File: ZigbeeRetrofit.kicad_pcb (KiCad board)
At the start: 2 copper layers, 20 x 50 mm, 24 parts, among them J1 110990030, J2 U.FL-R-SMT-1(10), J3 TC2050-IDC-NL, U1 CC2531F256RHAT, U2 SPX3819M5-L-3-3, Y1 32 Mhz, Y2 ECS-.327-12.5-34RR-TR

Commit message: Updated layout with 3d models
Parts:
- moved J3 19.3 mm to (107.4, 58.8), turned to 90 degrees
- moved C7 7.81 mm to (117.3, 77.4)
- moved C2 7.39 mm to (116.4, 68.3), turned to 0 degrees
- moved C6 7.15 mm to (113.0, 73.2)
- moved L1 7.15 mm to (116.5, 72.2)
- moved L2 7.15 mm to (113.0, 71.2)
- moved U1 7.15 mm to (104.5, 74.7)
- moved Y1 7.15 mm to (117.7, 80.5)
- moved C8 7.15 mm to (102.2, 69.1)
- moved R1 7.15 mm to (109.8, 72.3)
- moved C4 6.85 mm to (118.0, 84.0)
- moved C3 6.84 mm to (116.5, 74.6)
- moved C5 6.84 mm to (113.0, 74.6)
- moved C12 6.79 mm to (105.0, 63.6)
- moved Y2 6.79 mm to (106.3, 66.8)
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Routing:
- net /RESET: track 0.00 -> 51.9 mm, vias 0 -> 2
- net /DC: track 0.00 -> 20.5 mm, vias 0 -> 2
- net /DD: track 0.00 -> 19.1 mm
- net Net-(C1-Pad1): track 18.1 -> 29.5 mm
- net /TX: track 29.7 -> 22.5 mm
- net /RX: track 27.8 -> 20.7 mm
- net +5V: track 32.1 -> 36.0 mm
- net Net-(C2-Pad1): track 3.95 -> 6.68 mm
- net +3.3V: track 48.0 -> 49.4 mm, vias 5 -> 6
- net Net-(C7-Pad1): track 12.9 -> 12.3 mm
- net Net-(C11-Pad1): track 7.45 -> 8.12 mm
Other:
- outline, holes or cut-outs redrawn

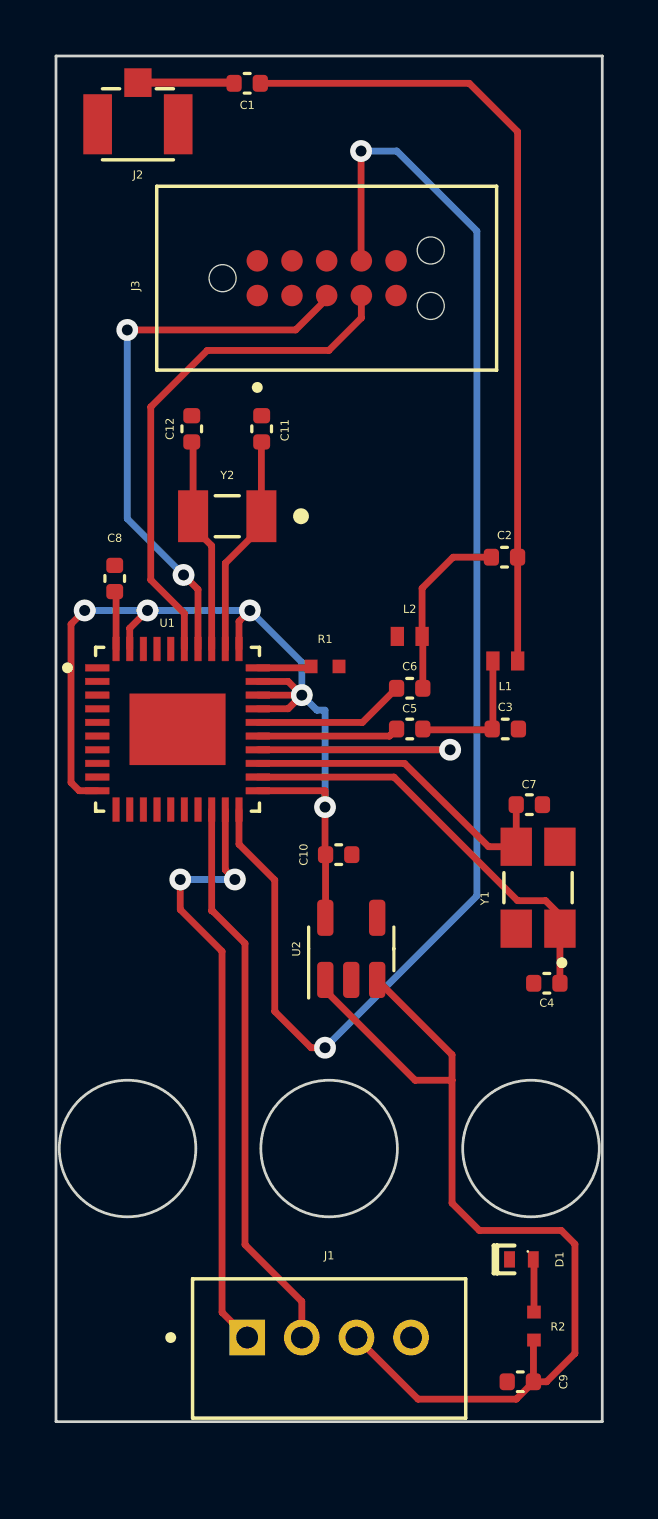
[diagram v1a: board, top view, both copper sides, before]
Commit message: Added ground
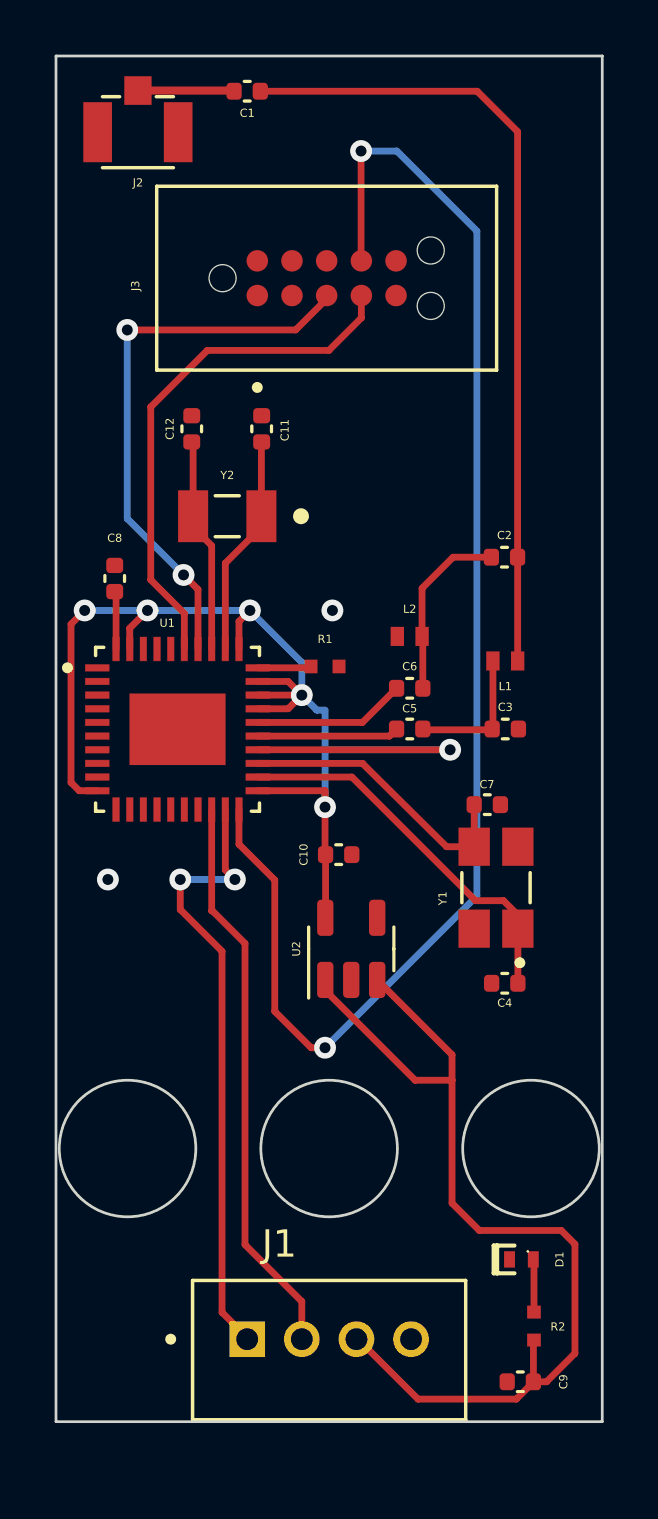
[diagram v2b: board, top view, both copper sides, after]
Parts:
- moved Y1 1.54 mm to (116.1, 80.5)
- moved C4 1.54 mm to (116.4, 84.0)
- moved C7 1.54 mm to (115.8, 77.4)
- moved C1 0.29 mm to (107.0, 51.3)
- moved J2 0.29 mm to (103.0, 52.8)
- moved J1 0.06 mm to (110.0, 97.0)
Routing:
- net Net-(C4-Pad1): track 15.7 -> 14.1 mm
- net Net-(C7-Pad1): track 12.3 -> 10.7 mm
- net GND: vias 0 -> 2
- added copper zone on B.Cu, net GND
- added copper zone on F.Cu, net GND
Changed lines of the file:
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@@
   )
   (footprint "Capacitor_SMD:C_0402_1005Metric" (layer "F.Cu")
-    (at 117.33 77.41)
+    (at 115.79 77.41)
     (descr "Capacitor SMD 0402 (1005 Metric), square (rectangular) end terminal, IPC_7351 nominal, (Body size source: IPC-SM-782 page 76, https://www.pcb-3d.com/wordpress/wp-content/uploads/ipc-sm-782a_amendment_1_and_2.pdf), generated with kicad-footprint-generator")
     (tags "capacitor")
@@
   )
   (footprint "ECS-320-13-42-CKM-TR:XTAL_ECS-320-13-42-CKM-TR" (layer "F.Cu")
-    (at 117.65 80.45 90)
+    (at 116.11 80.45 90)
     (property "MANUFACTURER" "ECS Inc.")
     (property "PARTREV" "11/11")
@@
   )
   (footprint "110990030:SEEED_110990030" (layer "F.Cu")
-    (at 110 96.92)
+    (at 110 96.98)
+    (property "Availability" "In Stock")
+    (property "Check_prices" "https://www.snapeda.com/parts/114020164/Seeed+Technology+Co.%252C+Ltd/view-part/?ref=eda")
+    (property "Description" "\nGROVE FEMALE HEADER R/A 20PACK\n")
     (property "MANUFACTURER" "Seeed Technology")
     (property "MAXIMUM_PACKAGE_HEIGHT" "8.1mm")
+    (property "MF" "Seeed Technology Co., Ltd")
+    (property "MP" "114020164")
     (property "PARTREV" "A")
+    (property "Package" "None")
+    (property "Price" "None")
+    (property "Purchase-URL" "https://www.snapeda.com/api/url_track_click_mouser/?unipart_id=5310052&manufacturer=Seeed Technology Co., Ltd&part_name=114020164&search_term=None")
     (property "STANDARD" "Manufacturer Recommendations")
     (property "Sheetfile" "ZigbeeRetrofit.kicad_sch")
     (property "Sheetname" "")
+    (property "SnapEDA_Link" "https://www.snapeda.com/parts/114020164/Seeed+Technology+Co.%252C+Ltd/view-part/?ref=snap")
     (attr through_hole)
-    (fp_text reference "J1" (at 0 -3) (layer "F.SilkS")
-      (effects (font (size 0.3 0.3) (thickness 0.05)))
+    (fp_text reference "J1" (at -1.825 -3.485) (layer "F.SilkS")
+      (effects (font (size 1 1) (thickness 0.15)))
     )
     (fp_text value "110990030" (at 4.525 4.385) (layer "F.Fab")
       (effects (font (size 1 1) (thickness 0.15)))
     )
+    (fp_line (start -5 2.95) (end -5 -2.15) (layer "F.SilkS") (width 0.127))
+    (fp_line (start 5 2.95) (end -5 2.95) (layer "F.SilkS") (width 0.127))
     (fp_line (start -5 -2.15) (end 5 -2.15) (layer "F.SilkS") (width 0.127))
-    (fp_line (start -5 2.95) (end -5 -2.15) (layer "F.SilkS") (width 0.127))
     (fp_line (start 5 -2.15) (end 5 2.95) (layer "F.SilkS") (width 0.127))
-    (fp_line (start 5 2.95) (end -5 2.95) (layer "F.SilkS") (width 0.127))
     (fp_circle (center -5.8 0) (end -5.7 0) (layer "F.SilkS") (width 0.2) (fill none))
     (fp_line (start -5.25 -2.4) (end 5.25 -2.4) (layer "F.CrtYd") (width 0.05))
@@
     (fp_line (start 5.25 -2.4) (end 5.25 3.2) (layer "F.CrtYd") (width 0.05))
     (fp_line (start 5.25 3.2) (end -5.25 3.2) (layer "F.CrtYd") (width 0.05))
+    (fp_line (start -5 -2.15) (end 5 -2.15) (layer "F.Fab") (width 0.127))
+    (fp_line (start 5 -2.15) (end 5 2.95) (layer "F.Fab") (width 0.127))
+    (fp_line (start -5 2.95) (end -5 -2.15) (layer "F.Fab") (width 0.127))
     (fp_line (start 5 2.95) (end -5 2.95) (layer "F.Fab") (width 0.127))
-    (fp_line (start 5 -2.15) (end 5 2.95) (layer "F.Fab") (width 0.127))
-    (fp_line (start -5 -2.15) (end 5 -2.15) (layer "F.Fab") (width 0.127))
-    (fp_line (start -5 2.95) (end -5 -2.15) (layer "F.Fab") (width 0.127))
     (fp_circle (center -5.8 0) (end -5.7 0) (layer "F.Fab") (width 0.2) (fill none))
     (pad "1" thru_hole rect locked (at -3 0) (size 1.308 1.308) (drill 0.8) (layers *.Cu *.Mask)
@@
     (pad "4" thru_hole circle locked (at 3 0) (size 1.308 1.308) (drill 0.8) (layers *.Cu *.Mask)
       (net 5 "GND") (pinfunction "4") (pintype "passive"))
-    (model "${KIPRJMOD}/110990030/110990030--3DModel-STEP-56544.STEP"
-      (offset (xyz 0 0 0))
-      (scale (xyz 1 1 1))
-      (rotate (xyz -90 0 0))
-    )
   )
   (footprint "Capacitor_SMD:C_0402_1005Metric" (layer "F.Cu")
@@
   )
   (footprint "Capacitor_SMD:C_0402_1005Metric" (layer "F.Cu")
-    (at 107 51 180)
+    (at 107 51.29 180)
     (descr "Capacitor SMD 0402 (1005 Metric), square (rectangular) end terminal, IPC_7351 nominal, (Body size source: IPC-SM-782 page 76, https://www.pcb-3d.com/wordpress/wp-content/uploads/ipc-sm-782a_amendment_1_and_2.pdf), generated with kicad-footprint-generator")
     (tags "capacitor")
@@
   )
   (footprint "Capacitor_SMD:C_0402_1005Metric" (layer "F.Cu")
-    (at 117.97 83.95 180)
+    (at 116.43 83.95 180)
     (descr "Capacitor SMD 0402 (1005 Metric), square (rectangular) end terminal, IPC_7351 nominal, (Body size source: IPC-SM-782 page 76, https://www.pcb-3d.com/wordpress/wp-content/uploads/ipc-sm-782a_amendment_1_and_2.pdf), generated with kicad-footprint-generator")
     (tags "capacitor")
@@
   )
   (footprint "U:HRS_U.FL-R-SMT-1(10)" (layer "F.Cu")
-    (at 103 52.5 180)
+    (at 103 52.79 180)
     (property "AVAILABILITY" "Good")
     (property "DESCRIPTION" "U.FL Series 6 Ghz 50 Ohm Ultra-small SMT Coaxial Cable Receptacle")
@@
       (polygon
         (pts
-          (xy 103.950158 53.6)
-          (xy 102.05 53.6)
-          (xy 102.05 51.49983)
-          (xy 103.950158 51.49983)
+          (xy 103.950158 53.89)
+          (xy 102.05 53.89)
+          (xy 102.05 51.78983)
+          (xy 103.950158 51.78983)
         )
       )
@@
   (gr_line (start 120 50) (end 100 50) (layer "Edge.Cuts") (width 0.1))
   (segment (start 116.903 68.353) (end 116.9 68.35) (width 0.25) (layer "F.Cu") (net 1))
-  (segment (start 115.13 51) (end 107.48 51) (width 0.25) (layer "F.Cu") (net 1))
+  (segment (start 115.42 51.29) (end 107.48 51.29) (width 0.25) (layer "F.Cu") (net 1))
   (segment (start 116.903 72.15) (end 116.903 68.353) (width 0.25) (layer "F.Cu") (net 1))
-  (segment (start 116.9 52.77) (end 115.13 51) (width 0.25) (layer "F.Cu") (net 1))
+  (segment (start 116.9 52.77) (end 115.42 51.29) (width 0.25) (layer "F.Cu") (net 1))
   (segment (start 116.9 68.35) (end 116.9 52.77) (width 0.25) (layer "F.Cu") (net 1))
-  (segment (start 106.495 50.975) (end 106.52 51) (width 0.25) (layer "F.Cu") (net 2))
-  (segment (start 103 50.975) (end 106.495 50.975) (width 0.3) (layer "F.Cu") (net 2))
+  (segment (start 103 51.265) (end 106.495 51.265) (width 0.3) (layer "F.Cu") (net 2))
   (segment (start 114.54 68.35) (end 115.94 68.35) (width 0.25) (layer "F.Cu") (net 3))
   (segment (start 113.403 71.25) (end 113.403 69.487) (width 0.25) (layer "F.Cu") (net 3))
@@
   (segment (start 115.997 74.613) (end 115.997 72.15) (width 0.25) (layer "F.Cu") (net 4))
   (segment (start 113.43 74.67) (end 115.97 74.67) (width 0.25) (layer "F.Cu") (net 4))
-  (segment (start 107.39 76.4) (end 112.375 76.4) (width 0.25) (layer "F.Cu") (net 6))
-  (segment (start 116.9 80.925) (end 117.925 80.925) (width 0.25) (layer "F.Cu") (net 6))
-  (segment (start 118.45 81.45) (end 118.45 81.95) (width 0.25) (layer "F.Cu") (net 6))
-  (segment (start 112.375 76.4) (end 116.9 80.925) (width 0.25) (layer "F.Cu") (net 6))
-  (segment (start 117.925 80.925) (end 118.45 81.45) (width 0.25) (layer "F.Cu") (net 6))
-  (segment (start 118.45 81.95) (end 118.45 83.95) (width 0.25) (layer "F.Cu") (net 6))
+  (via (at 110.12 70.3) (size 0.8) (drill 0.4) (layers "F.Cu" "B.Cu") (free) (net 5))
+  (via (at 101.9 80.15) (size 0.8) (drill 0.4) (layers "F.Cu" "B.Cu") (free) (net 5))
+  (segment (start 115.36 80.925) (end 116.385 80.925) (width 0.25) (layer "F.Cu") (net 6))
+  (segment (start 116.91 81.45) (end 116.91 81.95) (width 0.25) (layer "F.Cu") (net 6))
+  (segment (start 110.835 76.4) (end 115.36 80.925) (width 0.25) (layer "F.Cu") (net 6))
+  (segment (start 107.39 76.4) (end 110.84 76.4) (width 0.25) (layer "F.Cu") (net 6))
+  (segment (start 116.385 80.925) (end 116.91 81.45) (width 0.25) (layer "F.Cu") (net 6))
+  (segment (start 116.91 81.95) (end 116.91 83.95) (width 0.25) (layer "F.Cu") (net 6))
   (segment (start 107.39 74.9) (end 112.21 74.9) (width 0.25) (layer "F.Cu") (net 7))
   (segment (start 112.21 74.9) (end 112.47 74.64) (width 0.25) (layer "F.Cu") (net 7))
   (segment (start 111.22 74.4) (end 112.47 73.15) (width 0.25) (layer "F.Cu") (net 8))
   (segment (start 107.39 74.4) (end 111.22 74.4) (width 0.25) (layer "F.Cu") (net 8))
-  (segment (start 116.85 77.41) (end 116.85 78.95) (width 0.25) (layer "F.Cu") (net 9))
-  (segment (start 107.39 75.9) (end 112.76 75.9) (width 0.25) (layer "F.Cu") (net 9))
-  (segment (start 115.84 78.95) (end 116.85 78.95) (width 0.25) (layer "F.Cu") (net 9))
-  (segment (start 112.76 75.9) (end 115.84 78.95) (width 0.25) (layer "F.Cu") (net 9))
+  (segment (start 115.31 77.41) (end 115.31 78.95) (width 0.25) (layer "F.Cu") (net 9))
+  (segment (start 114.3 78.95) (end 115.31 78.95) (width 0.25) (layer "F.Cu") (net 9))
+  (segment (start 107.39 75.9) (end 111.23 75.9) (width 0.25) (layer "F.Cu") (net 9))
+  (segment (start 111.22 75.9) (end 114.3 78.95) (width 0.25) (layer "F.Cu") (net 9))
   (segment (start 102.2 69.66) (end 102.15 69.61) (width 0.25) (layer "F.Cu") (net 10))
   (segment (start 102.2 71.71) (end 102.2 69.66) (width 0.25) (layer "F.Cu") (net 10))
@@
   (segment (start 109.288 72.4) (end 109.338 72.35) (width 0.25) (layer "F.Cu") (net 27))
   (segment (start 107.39 72.4) (end 109.288 72.4) (width 0.25) (layer "F.Cu") (net 27))
+  (zone (net 5) (net_name "GND") (layers F&B.Cu) (hatch edge 0.508)
+    (connect_pads (clearance 0.508))
+    (min_thickness 0.254) (filled_areas_thickness no)
+    (fill yes (thermal_gap 0.508) (thermal_bridge_width 0.508))
+    (polygon
+      (pts
+        (xy 119.99 100)
+        (xy 100 100.01)
+        (xy 100.01 50.01)
+        (xy 120 50.01)
+      )
+    )
+  )
 )

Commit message: Updated grove connector
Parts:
- J1: value 110990030 -> 110990037; footprint 110990030:SEEED_110990030 -> Connector_JST:JST_PH_S4B-PH-K_1x04_P2.00mm_Horizontal
- moved J1 3.51 mm to (107.0, 95.2)
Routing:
- net /TX: track 22.5 -> 20.6 mm
- net /RX: track 20.7 -> 18.9 mm
- net +5V: track 36.0 -> 37.8 mm
- net GND: vias 2 -> 5
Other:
- outline, holes or cut-outs redrawn
- board text added: "Zigbee Retrofit Rev: 0.1"
- board text added: "by Timothy Findlay"
- board text added: "designed 2023-08-13"

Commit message: Revision 0.2 - Draft
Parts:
- moved C2 2.92 mm to (116.4, 71.3)
- moved D1 1.81 mm to (117.5, 95.8)
- moved R2 1.42 mm to (117.9, 97.8)
- moved L1 0.79 mm to (116.5, 72.9)
- moved C9 0.72 mm to (116.7, 97.9), turned to 90 degrees
- moved C8 0.54 mm to (102.2, 68.6)
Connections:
- J3 pad 2: unconnected-(J3-Pad2) -> +3.3V
- J3 pad 9: unconnected-(J3-Pad9) -> +3.3V
- U1 pad 41: unconnected-(U1-Pad41) -> GND
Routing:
- net +3.3V: track 49.4 -> 75.3 mm, vias 6 -> 8
- net GND: track 0.00 -> 9.27 mm, vias 5 -> 9
- net /DC: track 20.4 -> 15.3 mm
- net +5V: track 37.8 -> 32.7 mm
- net /TX: track 20.6 -> 17.9 mm, vias 2 -> 0
- net Net-(C2-Pad1): track 6.68 -> 4.46 mm
- net Net-(C1-Pad1): track 29.4 -> 30.2 mm
- net Net-(C3-Pad1): track 5.04 -> 4.30 mm
- net /RX: track 18.9 -> 19.6 mm, vias 0 -> 2
- net Net-(C8-Pad1): track 2.12 -> 2.64 mm
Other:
- outline, holes or cut-outs redrawn
- board text added: "+5"
- board text added: "GND"
- board text added: "RX"
- board text added: "TX"
- board text added: "Zigbee Retrofit Rev: 0.2"
- board text added: "designed 2023-10-14"
- board text removed: "Zigbee Retrofit Rev: 0.1"
- board text removed: "designed 2023-08-13"

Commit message: Revision 0.2 - Final
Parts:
- R1: value ERJ-2GEJ563X -> 56K Ohm
- R2: value ERJ-2GEJ151X -> 150 Ohm
- moved L2 1.41 mm to (114.4, 71.2)
- moved C5 1.40 mm to (114.3, 74.6)
- moved C6 1.40 mm to (114.3, 73.2)
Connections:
- J1 pad 1: /TX -> GND
- J1 pad 2: /RX -> +5V
- J1 pad 3: +5V -> /RX
- J1 pad 4: GND -> /TX
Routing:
- net +3.3V: track 75.3 -> 65.8 mm
- net /RESET: track 51.9 -> 46.6 mm
- net /TX: track 17.9 -> 22.7 mm
- net +5V: track 32.7 -> 34.6 mm
- net Net-(C2-Pad1): track 4.46 -> 2.99 mm
- net Net-(C3-Pad1): track 4.30 -> 2.83 mm
- net Net-(C6-Pad1): track 5.60 -> 6.98 mm
- net Net-(C5-Pad1): track 5.19 -> 6.52 mm
- net /RX: track 19.6 -> 20.8 mm, vias 2 -> 1
- net GND: vias 9 -> 10
